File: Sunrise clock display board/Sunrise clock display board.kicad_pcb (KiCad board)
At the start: 2 copper layers, 160 x 45.7 mm, 21 parts, among them J1 Conn_02x05_Odd_Even, Q1 2N7002, U1 Nokia_5110_display, U2 Nokia_5110_display, U3 Nokia_5110_display

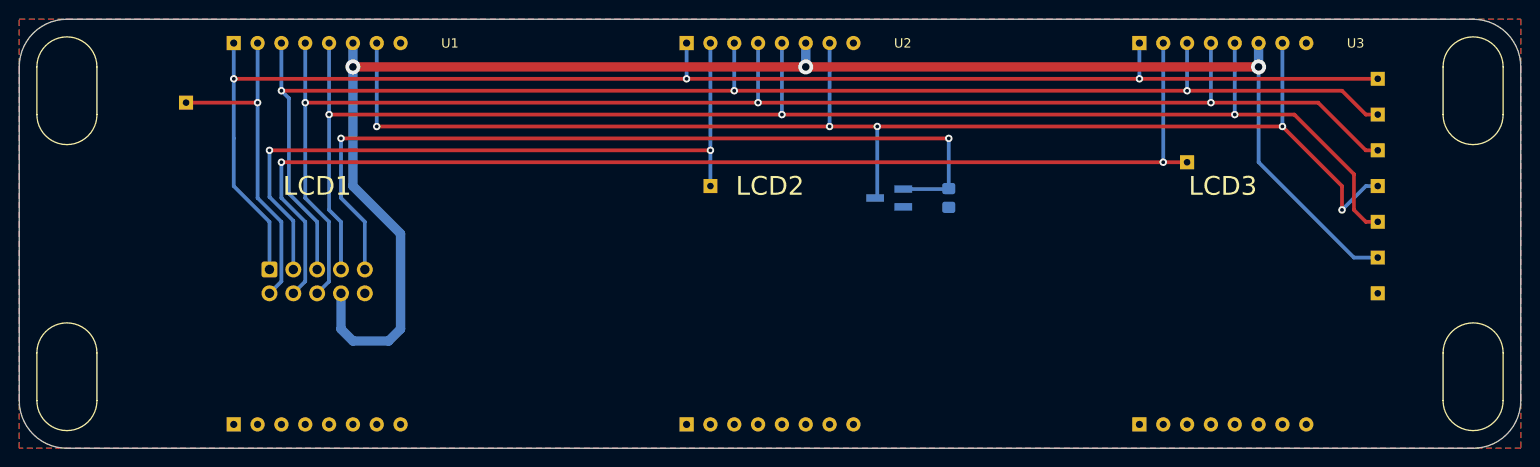
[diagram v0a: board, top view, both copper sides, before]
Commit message: Update to Kicad 6.
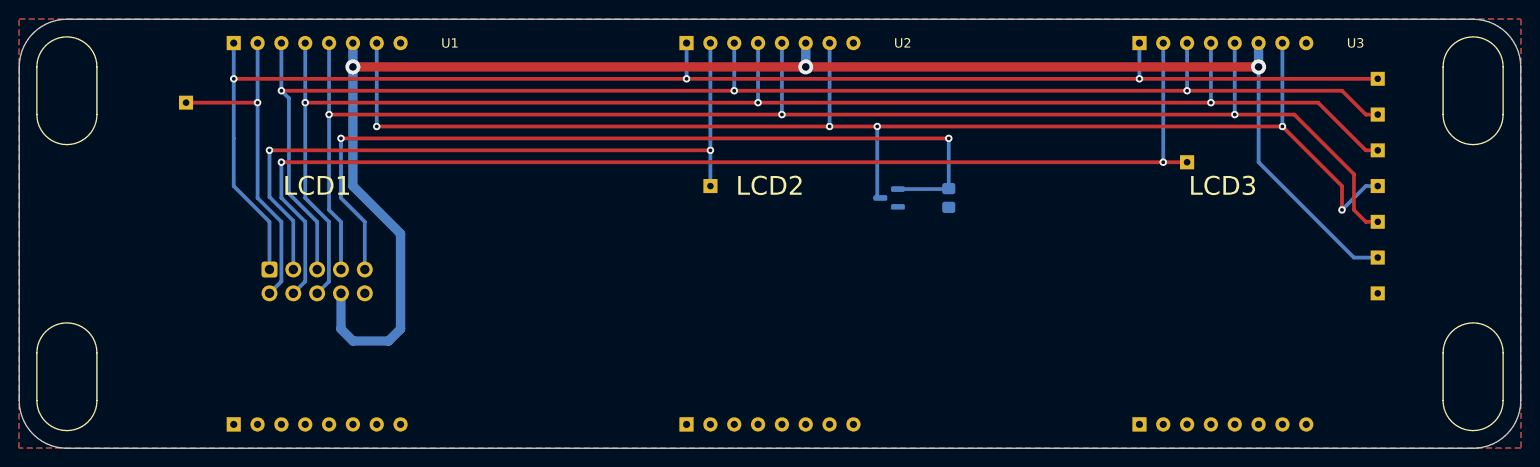
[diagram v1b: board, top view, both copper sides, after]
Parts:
- Q1: footprint Package_TO_SOT_SMD:SOT-23_Handsoldering -> Package_TO_SOT_SMD:SOT-23
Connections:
- net LCD1_~CE renamed LCD1_~{CE}
- net LCD2_~CE renamed LCD2_~{CE}
- net LCD3_~CE renamed LCD3_~{CE}
- net LCD_DATA-~CMD renamed LCD_DATA-~{CMD}
- net LCD_FET_~LED renamed LCD_FET_~{LED}
- net LCD_~RST renamed LCD_~{RST}
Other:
- net class Default removed
- board text added: "LCD1_~{CE}"
- board text added: "LCD2_~{CE}"
- board text added: "LCD3_~{CE}"
- board text added: "LCD_DATA-~{CMD}"
- board text added: "LCD_FET_~{LED}"
- board text added: "LCD_~{RST}"
- board text removed: "LCD1_~CE"
- board text removed: "LCD2_~CE"
- board text removed: "LCD3_~CE"
- board text removed: "LCD_DATA-~CMD"
- board text removed: "LCD_FET_~LED"
- board text removed: "LCD_~RST"
